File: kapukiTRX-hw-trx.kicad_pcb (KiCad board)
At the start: 4 copper layers, 45.7 x 27.9 mm, 88 parts, among them J1 GPS, J10 Conn_01x01, J11 Conn_01x01, J12 Conn_01x01, J13 Conn_01x01, J14 Conn_01x01, J15 Conn_01x01, J16 Conn_01x01, J17 Conn_01x01, J18 Conn_01x01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

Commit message: Swap pwm lines for better routing
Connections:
- U1 pad A10: /PWM7 -> /PWM4
- U1 pad A4: Net-(U1-PadA4) -> /TXMODE
- U1 pad A6: /PWM3 -> /PWM1
- U1 pad A7: /TXMODE -> Net-(U1-PadA7)
- U1 pad A8: /PWM2 -> /PWM3
- U1 pad B6: /PWM4 -> /PWM2
- U1 pad B9: /PWM1 -> /PWM5
- U1 pad G4: /PWM5 -> /PWM7
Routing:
- net /PWM4: track 4.85 -> 0.00 mm
- net /PWM1: track 1.55 -> 4.45 mm
- net /PWM2: track 2.49 -> 4.85 mm
- net /PWM3: track 4.45 -> 2.49 mm
- net /PWM5: track 0.00 -> 1.55 mm
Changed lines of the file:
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@@
-(kicad_pcb (version 20171130) (host pcbnew "(5.1.4)-1")
+(kicad_pcb (version 20171130) (host pcbnew "(5.1.4-0-10_14)")
   (general
     (thickness 1.6)
@@
   (net 126 "Net-(U1-PadB5)")
   (net 127 "Net-(U1-PadB4)")
-  (net 128 "Net-(U1-PadA4)")
+  (net 128 "Net-(U1-PadA7)")
   (net_class Default "This is the default net class."
     (clearance 0.127)
@@
     (add_net "Net-(R5-Pad1)")
     (add_net "Net-(R8-Pad1)")
-    (add_net "Net-(U1-PadA4)")
+    (add_net "Net-(U1-PadA7)")
     (add_net "Net-(U1-PadA9)")
     (add_net "Net-(U1-PadB3)")
@@
       (net 35 /SWCLK))
     (pad A10 smd circle (at 3.6 -3.6) (size 0.36 0.36) (layers F.Cu F.Paste F.Mask)
-      (net 46 /PWM7))
+      (net 49 /PWM4))
     (pad K9 smd circle (at 2.8 3.6) (size 0.36 0.36) (layers F.Cu F.Paste F.Mask)
       (net 11 /RF1MOSI))
@@
       (net 86 "Net-(U1-PadC9)"))
     (pad B9 smd circle (at 2.8 -2.8) (size 0.36 0.36) (layers F.Cu F.Paste F.Mask)
-      (net 53 /PWM1))
+      (net 48 /PWM5))
     (pad A9 smd circle (at 2.8 -3.6) (size 0.36 0.36) (layers F.Cu F.Paste F.Mask)
       (net 87 "Net-(U1-PadA9)"))
@@
       (net 92 "Net-(U1-PadB8)"))
     (pad A8 smd circle (at 2 -3.6) (size 0.36 0.36) (layers F.Cu F.Paste F.Mask)
-      (net 54 /PWM2))
+      (net 50 /PWM3))
     (pad K7 smd circle (at 1.2 3.6) (size 0.36 0.36) (layers F.Cu F.Paste F.Mask)
       (net 8 /RF1RXEN))
@@
       (net 96 "Net-(U1-PadB7)"))
     (pad A7 smd circle (at 1.2 -3.6) (size 0.36 0.36) (layers F.Cu F.Paste F.Mask)
-      (net 119 /TXMODE))
+      (net 128 "Net-(U1-PadA7)"))
     (pad K6 smd circle (at 0.4 3.6) (size 0.36 0.36) (layers F.Cu F.Paste F.Mask)
       (net 22 /RF2IRQ))
@@
       (net 100 "Net-(U1-PadC6)"))
     (pad B6 smd circle (at 0.4 -2.8) (size 0.36 0.36) (layers F.Cu F.Paste F.Mask)
-      (net 49 /PWM4))
+      (net 54 /PWM2))
     (pad A6 smd circle (at 0.4 -3.6) (size 0.36 0.36) (layers F.Cu F.Paste F.Mask)
-      (net 50 /PWM3))
+      (net 53 /PWM1))
     (pad K5 smd circle (at -0.4 3.6) (size 0.36 0.36) (layers F.Cu F.Paste F.Mask)
       (net 101 "Net-(U1-PadK5)"))
@@
       (net 55 /RFPOWEREN))
     (pad G4 smd circle (at -1.2 1.2) (size 0.36 0.36) (layers F.Cu F.Paste F.Mask)
-      (net 48 /PWM5))
+      (net 46 /PWM7))
     (pad F4 smd circle (at -1.2 0.4) (size 0.36 0.36) (layers F.Cu F.Paste F.Mask)
       (net 105 "Net-(U1-PadF4)"))
@@
       (net 127 "Net-(U1-PadB4)"))
     (pad A4 smd circle (at -1.2 -3.6) (size 0.36 0.36) (layers F.Cu F.Paste F.Mask)
-      (net 128 "Net-(U1-PadA4)"))
+      (net 119 /TXMODE))
     (pad K3 smd circle (at -2 3.6) (size 0.36 0.36) (layers F.Cu F.Paste F.Mask)
       (net 19 /RF2TXEN))
@@
   (segment (start 201.3458 110.005) (end 203.05 110.005) (width 0.127) (layer F.Cu) (net 44))
   (segment (start 203.05 110.005) (end 203.073 109.982) (width 0.127) (layer F.Cu) (net 44))
-  (segment (start 194.191501 95.976157) (end 195.044658 95.123) (width 0.127) (layer F.Cu) (net 49))
-  (segment (start 194.191501 96.524499) (end 194.191501 95.976157) (width 0.127) (layer F.Cu) (net 49))
-  (segment (start 193.821 96.895) (end 194.191501 96.524499) (width 0.127) (layer F.Cu) (net 49))
-  (segment (start 195.044658 95.123) (end 197.612 95.123) (width 0.127) (layer F.Cu) (net 49))
-  (segment (start 194.792452 94.86899) (end 194.939444 94.86899) (width 0.127) (layer F.Cu) (net 50))
-  (segment (start 193.821 95.840442) (end 194.792452 94.86899) (width 0.127) (layer F.Cu) (net 50))
-  (segment (start 193.821 96.095) (end 193.821 95.840442) (width 0.127) (layer F.Cu) (net 50))
-  (segment (start 194.939444 94.86899) (end 197.612 94.86899) (width 0.127) (layer F.Cu) (net 50))
-  (segment (start 196.221 96.895) (end 196.596 96.52) (width 0.127) (layer F.Cu) (net 53))
-  (segment (start 196.596 96.52) (end 197.612 96.52) (width 0.127) (layer F.Cu) (net 53))
-  (segment (start 195.421 96.095) (end 196.139 95.377) (width 0.127) (layer F.Cu) (net 54))
-  (segment (start 196.139 95.377) (end 197.612 95.377) (width 0.127) (layer F.Cu) (net 54))
+  (segment (start 194.191501 95.976157) (end 195.044658 95.123) (width 0.127) (layer F.Cu) (net 54))
+  (segment (start 194.191501 96.524499) (end 194.191501 95.976157) (width 0.127) (layer F.Cu) (net 54))
+  (segment (start 193.821 96.895) (end 194.191501 96.524499) (width 0.127) (layer F.Cu) (net 54))
+  (segment (start 195.044658 95.123) (end 197.612 95.123) (width 0.127) (layer F.Cu) (net 54))
+  (segment (start 194.792452 94.86899) (end 194.939444 94.86899) (width 0.127) (layer F.Cu) (net 53))
+  (segment (start 193.821 95.840442) (end 194.792452 94.86899) (width 0.127) (layer F.Cu) (net 53))
+  (segment (start 193.821 96.095) (end 193.821 95.840442) (width 0.127) (layer F.Cu) (net 53))
+  (segment (start 194.939444 94.86899) (end 197.612 94.86899) (width 0.127) (layer F.Cu) (net 53))
+  (segment (start 196.221 96.895) (end 196.596 96.52) (width 0.127) (layer F.Cu) (net 48))
+  (segment (start 196.596 96.52) (end 197.612 96.52) (width 0.127) (layer F.Cu) (net 48))
+  (segment (start 195.421 96.095) (end 196.139 95.377) (width 0.127) (layer F.Cu) (net 50))
+  (segment (start 196.139 95.377) (end 197.612 95.377) (width 0.127) (layer F.Cu) (net 50))
   (segment (start 189.566442 99.295) (end 189.560042 99.2886) (width 0.127) (layer F.Cu) (net 56))
   (segment (start 189.821 99.295) (end 189.566442 99.295) (width 0.127) (layer F.Cu) (net 56))

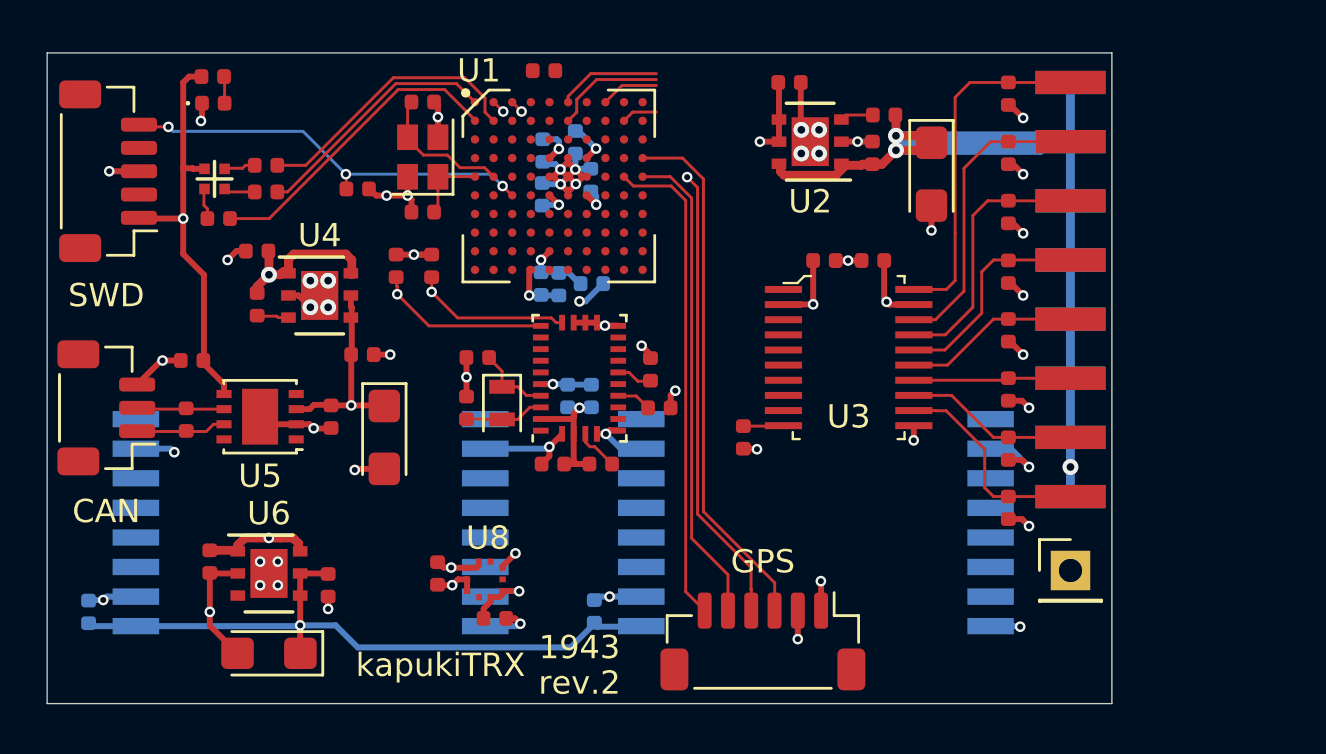
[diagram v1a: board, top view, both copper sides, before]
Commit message: Almost finish routing
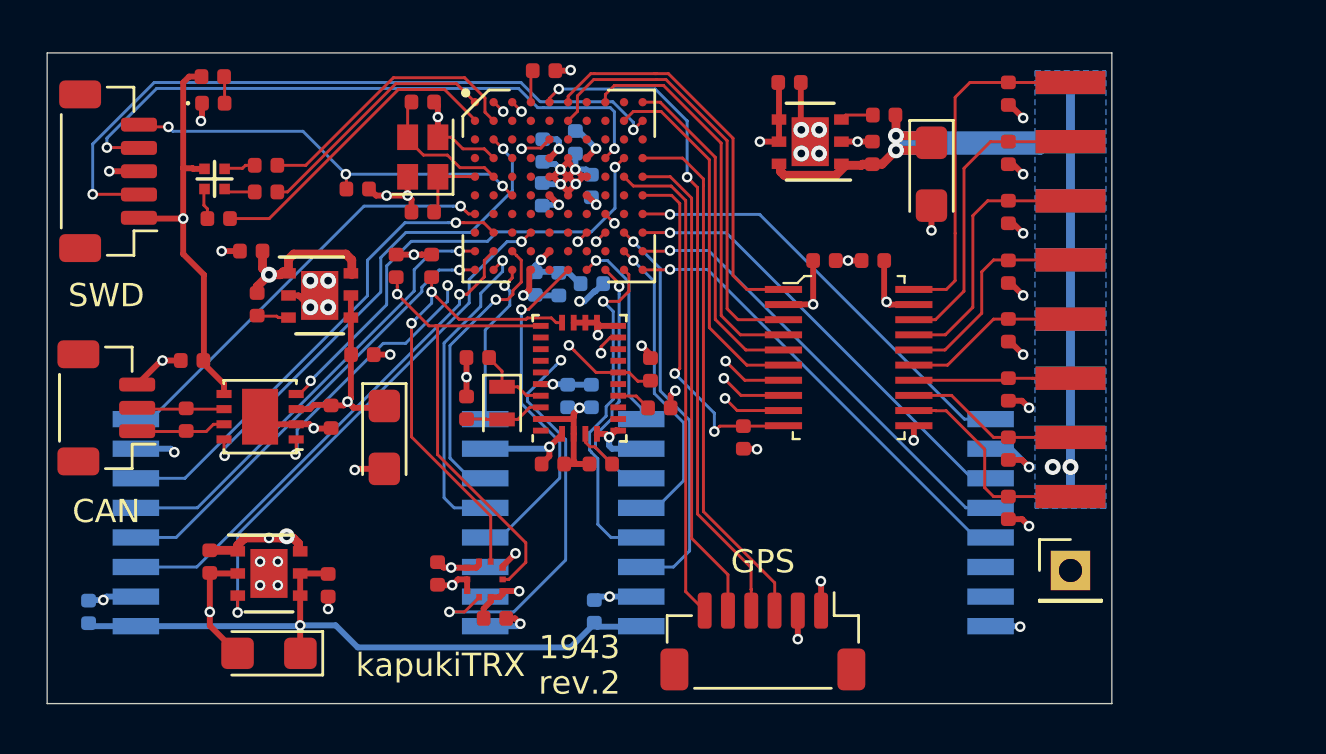
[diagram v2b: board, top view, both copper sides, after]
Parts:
- moved C7 0.26 mm to (194.8, 99.7)
- moved C23 0.25 mm to (180.2, 102.5)
- moved C8 0.25 mm to (192.4, 103.9)
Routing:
- net IN: track 106.8 -> 144.3 mm, vias 5 -> 7
- net /SWCLK: track 0.00 -> 30.0 mm, vias 0 -> 2
- net /SWDIO: track 0.00 -> 27.0 mm, vias 0 -> 2
- net /BMPINT: track 0.00 -> 25.7 mm, vias 0 -> 3
- net /RFPOWEREN: track 0.00 -> 22.6 mm, vias 0 -> 2
- net /RF2MISO: track 0.00 -> 21.6 mm, vias 0 -> 1
- net /CANEN: track 0.00 -> 21.4 mm, vias 0 -> 2
- net /RF2NSS: track 0.00 -> 21.1 mm, vias 0 -> 1
- net /CANRX: track 0.00 -> 20.3 mm, vias 0 -> 2
- net /CANTX: track 0.00 -> 19.7 mm, vias 0 -> 3
- net /RF1IRQ: track 0.00 -> 19.7 mm, vias 0 -> 1
- net /RF2CLK: track 0.00 -> 19.7 mm, vias 0 -> 1
- net /RF1BUSY: track 0.00 -> 19.5 mm, vias 0 -> 1
- net /RF2MOSI: track 0.00 -> 19.4 mm, vias 0 -> 1
- net /RF1NRESET: track 0.00 -> 19.3 mm, vias 0 -> 1
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- added copper zone on B.Cu, net IN

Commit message: Swap pwm lines for better routing
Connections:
- U1 pad E3: /PWM8 -> /PWM6
- U1 pad H1: /PWM6 -> /PWM8
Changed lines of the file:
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@@
-(kicad_pcb (version 20171130) (host pcbnew "(5.1.4)-1")
+(kicad_pcb (version 20171130) (host pcbnew "(5.1.4-0-10_14)")
   (general
     (thickness 1.6)
@@
       (net 32 /NRST))
     (pad E3 smd circle (at -2 -0.4) (size 0.36 0.36) (layers F.Cu F.Paste F.Mask)
-      (net 45 /PWM8))
+      (net 47 /PWM6))
     (pad D3 smd circle (at -2 -1.2) (size 0.36 0.36) (layers F.Cu F.Paste F.Mask)
       (net 111 "Net-(U1-PadD3)"))
@@
       (net 16 /RF2CLK))
     (pad H1 smd circle (at -3.6 2) (size 0.36 0.36) (layers F.Cu F.Paste F.Mask)
-      (net 47 /PWM6))
+      (net 45 /PWM8))
     (pad G1 smd circle (at -3.6 1.2) (size 0.36 0.36) (layers F.Cu F.Paste F.Mask)
       (net 18 /RF2RXEN))

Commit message: Finish routing
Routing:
- net /PWM8: track 2.72 -> 16.4 mm, vias 1 -> 2
- net /PWM6: track 2.82 -> 15.6 mm, vias 1 -> 2
- net /PWM7: track 2.86 -> 14.8 mm, vias 1 -> 2
- net /RF2BUSY: track 13.7 -> 12.2 mm
- added copper zone on B.Cu, net GND
- added copper zone on F.Cu, net GND
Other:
- net class VCC: via_dia 0.4572 -> 0.6858; via_drill 0.254 -> 0.3302

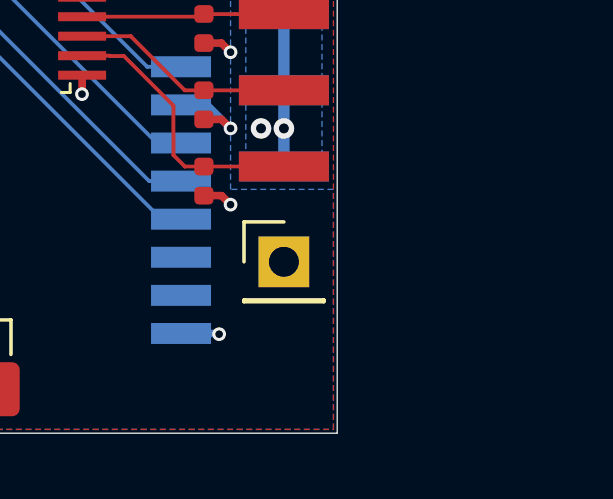
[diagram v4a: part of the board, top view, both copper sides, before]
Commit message: Add support for EX bus
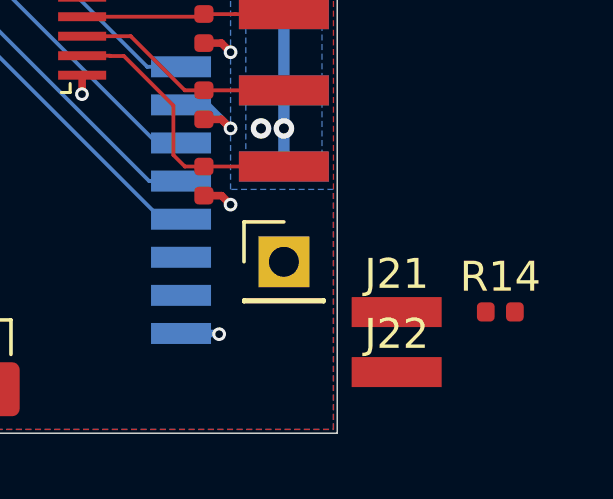
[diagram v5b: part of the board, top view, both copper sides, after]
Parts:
- added J21: Conn_01x01, miscellaneous:PinHeader_1x01_P1.27mm, F.Cu at (219.2, 117.9)
- added J22: Conn_01x01, miscellaneous:PinHeader_1x01_P1.27mm, F.Cu at (219.2, 119.9)
- added R14: 2k4, Resistor_SMD:R_0402_1005Metric, F.Cu at (222.6, 117.9)
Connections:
- U1 pad C7: Net-(U1-PadC7) -> /RXTX

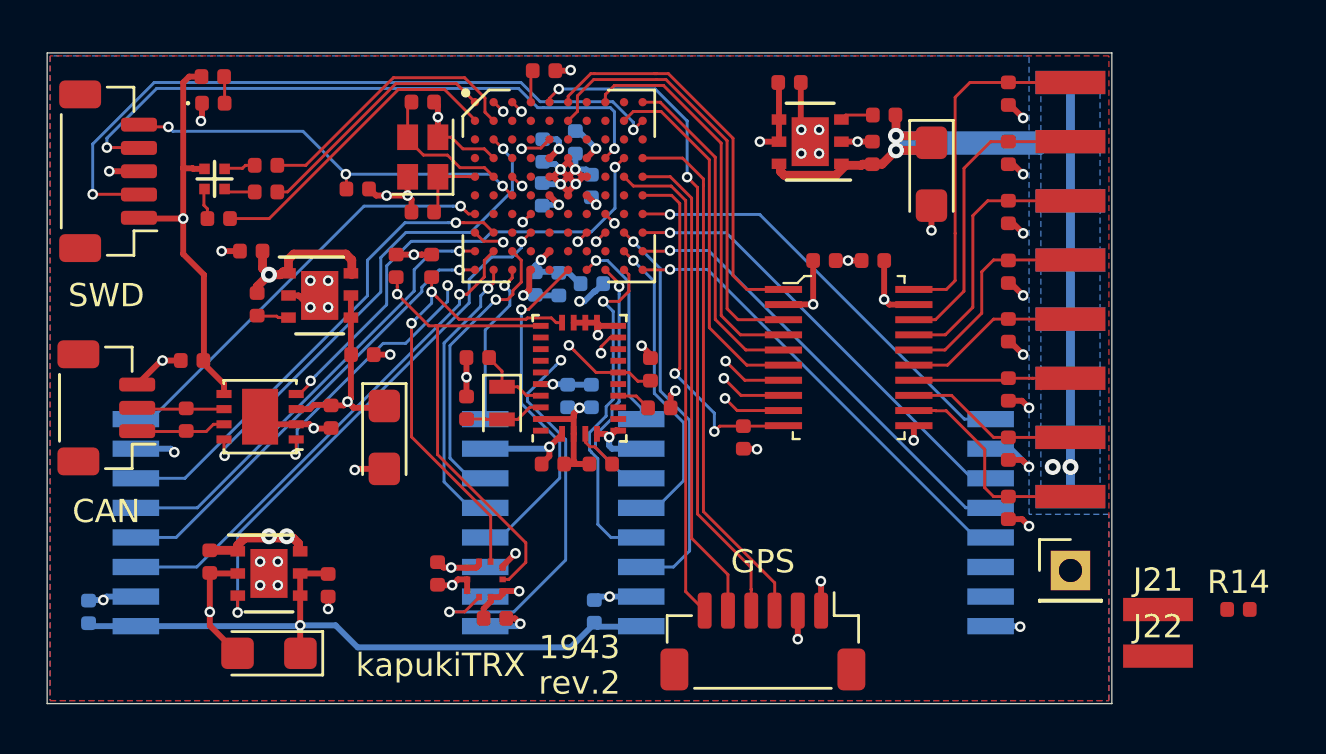
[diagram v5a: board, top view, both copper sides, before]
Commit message: Routing for EX bus
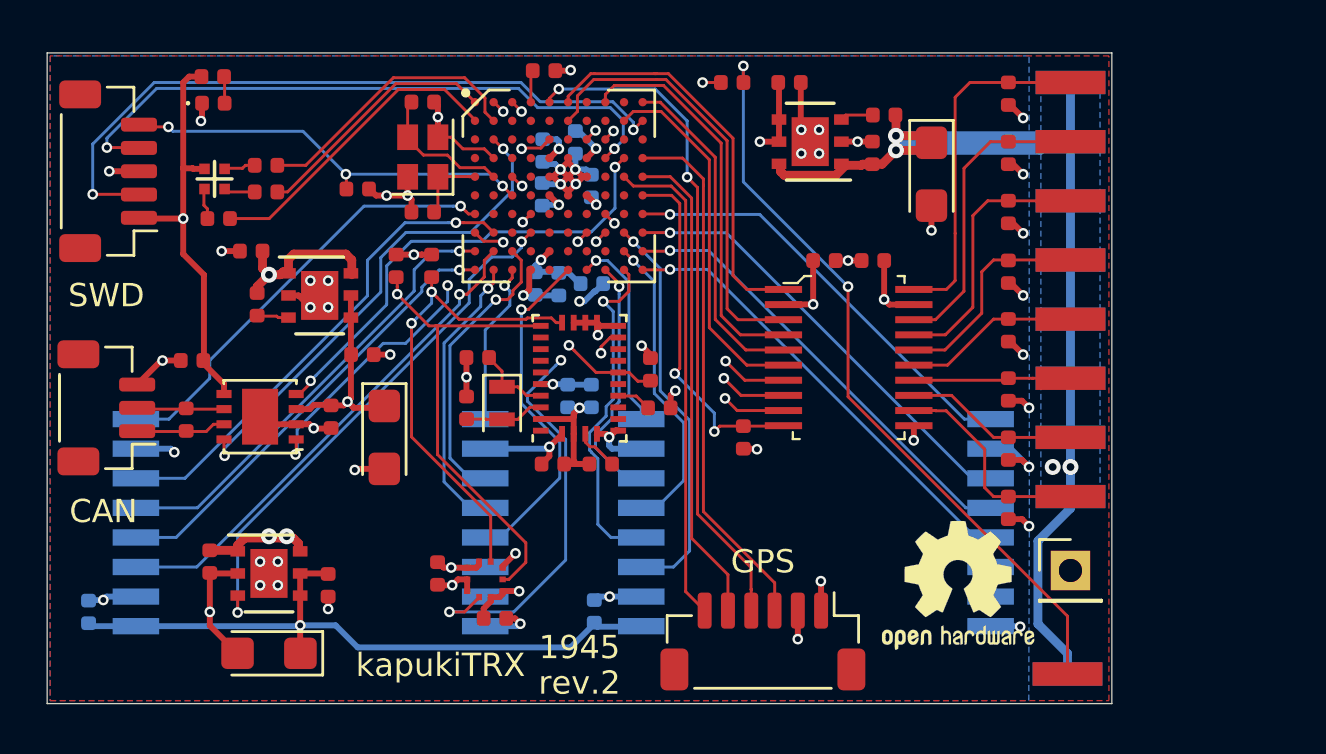
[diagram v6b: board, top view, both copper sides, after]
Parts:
- added REF**: OSHW-Logo2_7.3x6mm_SilkScreen, Symbol:OSHW-Logo2_7.3x6mm_SilkScreen, F.Cu at (210.6, 116.8)
- J21: moved to B.Cu
- moved R14 31.4 mm to (200.9, 95.2), turned to 180 degrees
- moved J21 4.77 mm to (215.3, 120.7)
- moved J22 3.96 mm to (215.3, 120.7)
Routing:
- net /RXTX: track 0.00 -> 40.6 mm, vias 0 -> 3
- net IN: track 144.4 -> 153.1 mm
- net Net-(R14-Pad2): track 0.00 -> 6.07 mm, vias 0 -> 2
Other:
- board text added: "1945"
- board text removed: "1943"

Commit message: Add an elec cap to cup rail
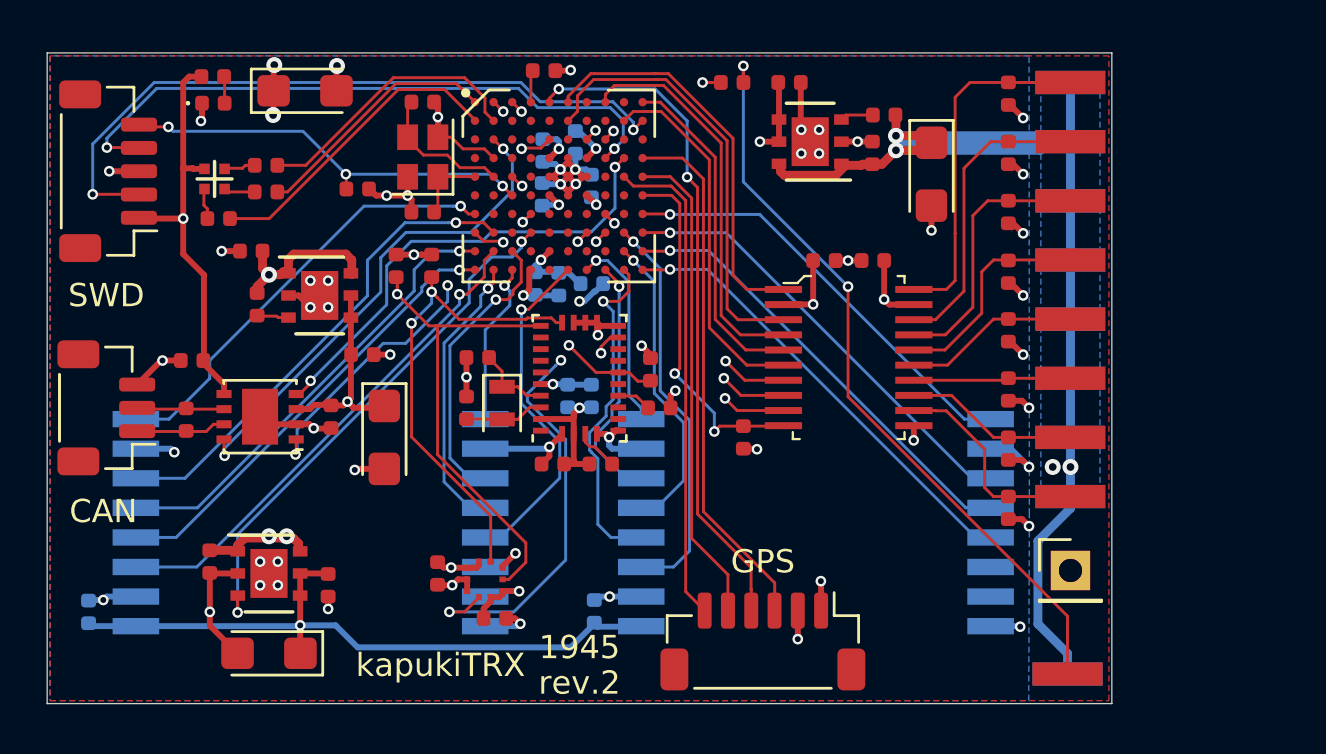
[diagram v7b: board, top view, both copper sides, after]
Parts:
- removed REF**: OSHW-Logo2_7.3x6mm_SilkScreen, Symbol:OSHW-Logo2_7.3x6mm_SilkScreen
- added C41: 10uF, Capacitor_Tantalum_SMD:CP_EIA-3216-18_Kemet-A, F.Cu at (182.5, 95.6)
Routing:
- net /VCCCPU: track 45.6 -> 47.7 mm, vias 14 -> 16
- net GND: track 82.8 -> 83.9 mm, vias 57 -> 58

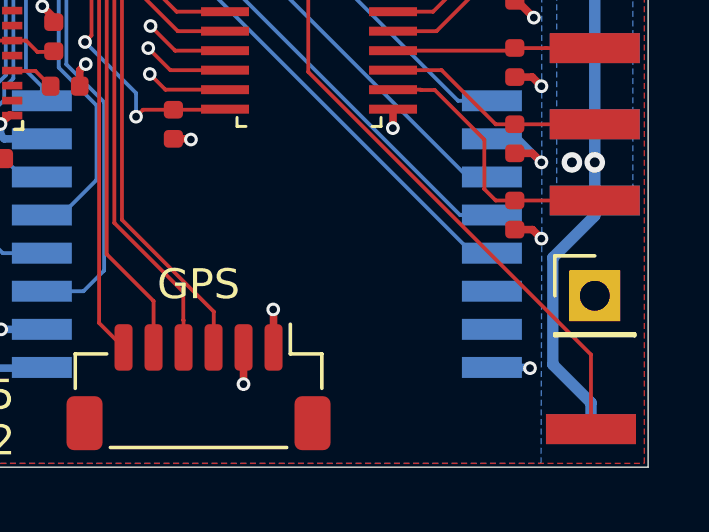
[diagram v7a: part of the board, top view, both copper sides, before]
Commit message: Add Open hardware logo
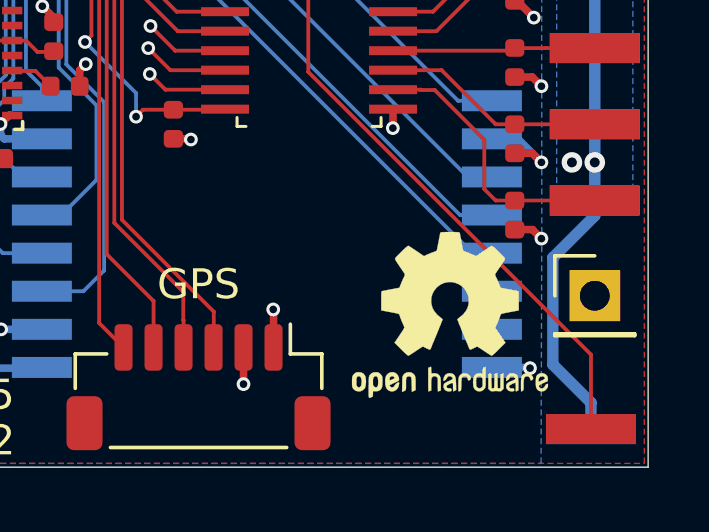
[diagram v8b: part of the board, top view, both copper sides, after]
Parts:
- added REF**: OSHW-Logo2_7.3x6mm_SilkScreen, Symbol:OSHW-Logo2_7.3x6mm_SilkScreen, F.Cu at (210.6, 116.8)
